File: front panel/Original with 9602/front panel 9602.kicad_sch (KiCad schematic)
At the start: 164 parts, among them J1 Accumulator, J10 Conn_01x04_Female, J11 Conn_01x04_Female, J12 Conn_01x04_Female, J13 ~EXT.LA, J14 Z-BIT, J2 Mem_Buffer, J3 Conn_01x16_Female, J4 Conn_01x04_Female, J5 Conn_01x04_Female, J6 Conn_01x04_Female, J7 SR_REGISTER, J8 Conn_01x04_Female, J9 Conn_01x04_Female, SW1 SR0, SW10 DEPOSIT, SW11 HALT, SW12 SINGLE, SW13 F/S, SW14 PAGE ZERO, SW15 RUN, SW16 EXAM, SW2 SR1, SW3 SR2, SW4 SR3, SW5 SR4, SW6 SR5, SW7 SR6, SW8 SR7, SW9 LD_ADDR, U1 74LS05, U10 DM9602, U11 74LS05, U12 74LS00, U2 74LS05, U3 74LS05, U4 74LS07, U5 74LS07, U6 74LS00, U7 74LS05, U8 74LS00, U9 74LS00

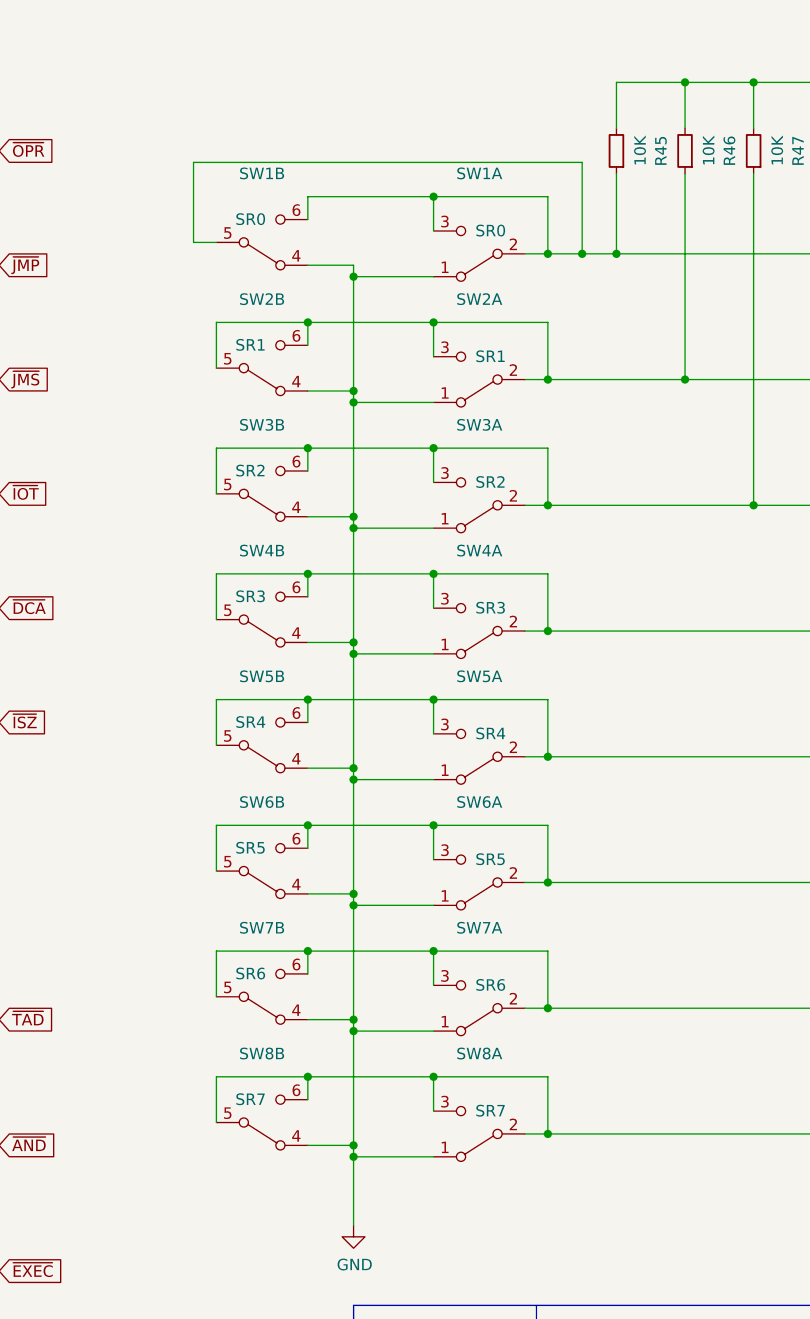
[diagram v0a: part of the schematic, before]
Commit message: New PCB with all the corrections made
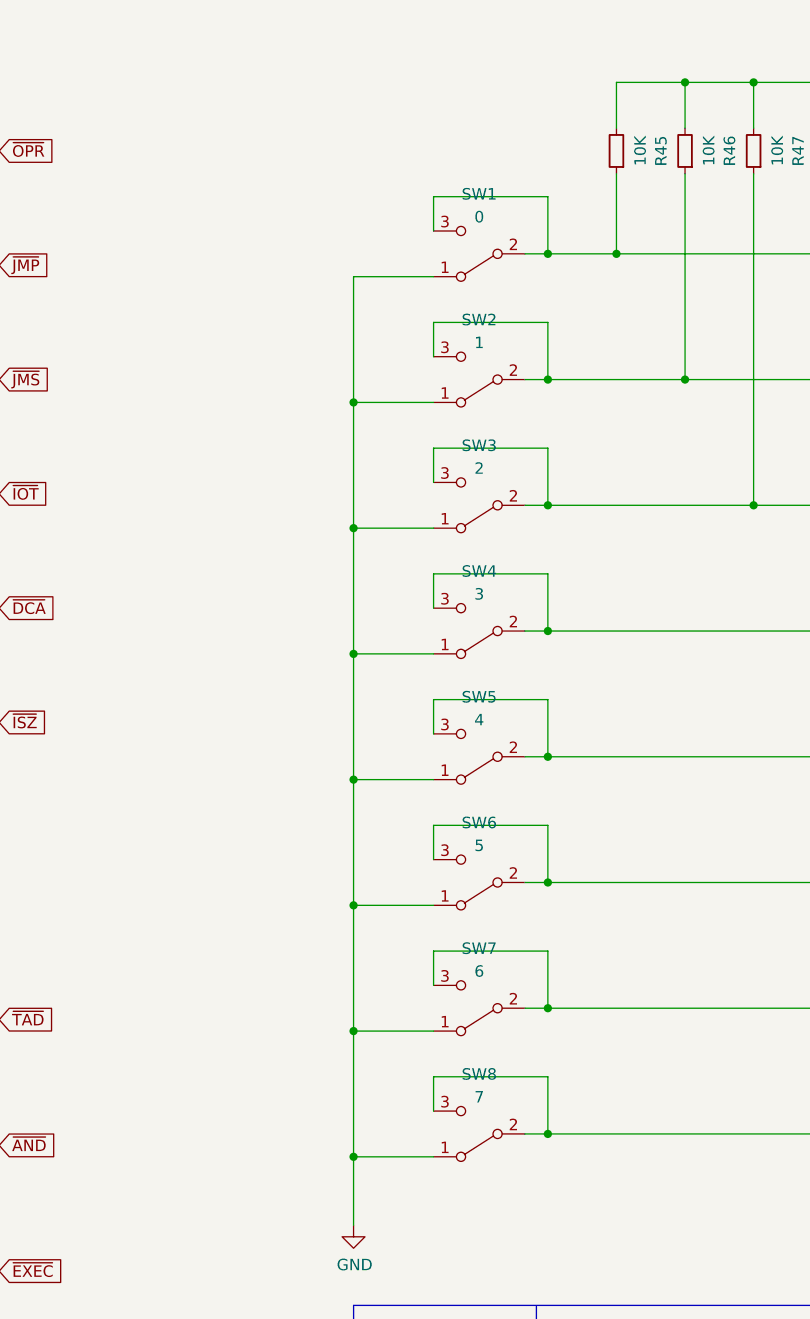
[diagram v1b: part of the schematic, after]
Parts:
- removed SW1: SR0, dBSound_library:DPDT_toggle_switch_wired, symbol Switch:SW_DPDT_x2
- removed SW2: SR1, dBSound_library:DPDT_toggle_switch_wired, symbol Switch:SW_DPDT_x2
- removed SW3: SR2, dBSound_library:DPDT_toggle_switch_wired, symbol Switch:SW_DPDT_x2
- removed SW4: SR3, dBSound_library:DPDT_toggle_switch_wired, symbol Switch:SW_DPDT_x2
- removed SW5: SR4, dBSound_library:DPDT_toggle_switch_wired, symbol Switch:SW_DPDT_x2
- removed SW6: SR5, dBSound_library:DPDT_toggle_switch_wired, symbol Switch:SW_DPDT_x2
- removed SW7: SR6, dBSound_library:DPDT_toggle_switch_wired, symbol Switch:SW_DPDT_x2
- removed SW8: SR7, dBSound_library:DPDT_toggle_switch_wired, symbol Switch:SW_DPDT_x2
- added SW1: 0, EDUC-8:SPDT_toggle_switch_wired, symbol Switch:SW_SPDT
- added SW2: 1, EDUC-8:SPDT_toggle_switch_wired, symbol Switch:SW_SPDT
- added SW3: 2, EDUC-8:SPDT_toggle_switch_wired, symbol Switch:SW_SPDT
- added SW4: 3, EDUC-8:SPDT_toggle_switch_wired, symbol Switch:SW_SPDT
- added SW5: 4, EDUC-8:SPDT_toggle_switch_wired, symbol Switch:SW_SPDT
- added SW6: 5, EDUC-8:SPDT_toggle_switch_wired, symbol Switch:SW_SPDT
- added SW7: 6, EDUC-8:SPDT_toggle_switch_wired, symbol Switch:SW_SPDT
- added SW8: 7, EDUC-8:SPDT_toggle_switch_wired, symbol Switch:SW_SPDT
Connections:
- net GND: now also SW1.1 (A), SW2.1 (A), SW3.1 (A), SW4.1 (A), SW5.1 (A), SW6.1 (A), SW7.1 (A), SW8.1 (A)
- net SR0: now also SW1.2 (B), SW1.3 (C)
- net SR1: now also SW2.2 (B), SW2.3 (C)
- net SR2: now also SW3.2 (B), SW3.3 (C)
- net SR3: now also SW4.2 (B), SW4.3 (C)
- net SR4: now also SW5.2 (B), SW5.3 (C)
- net SR5: now also SW6.2 (B), SW6.3 (C)
- net SR6: now also SW7.2 (B), SW7.3 (C)
- net SR7: now also SW8.2 (B), SW8.3 (C)

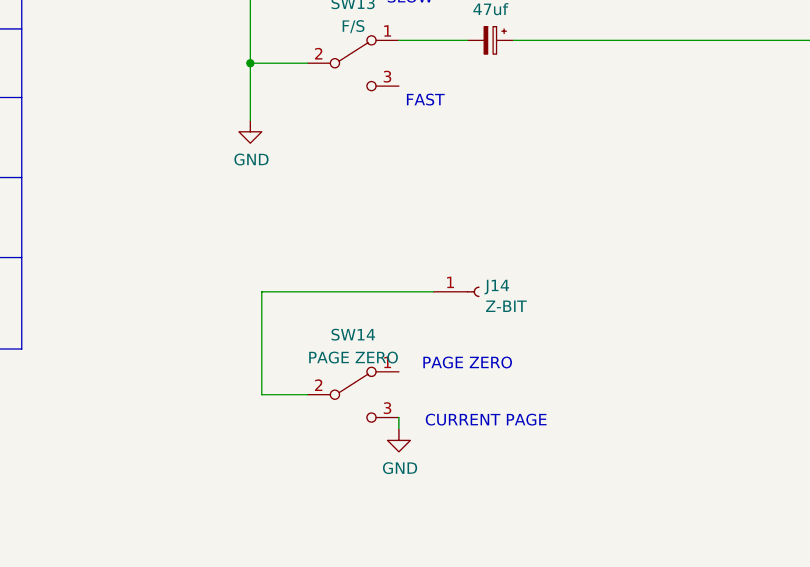
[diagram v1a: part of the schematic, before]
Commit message: Schematic update 2024-04-14 plus fixes
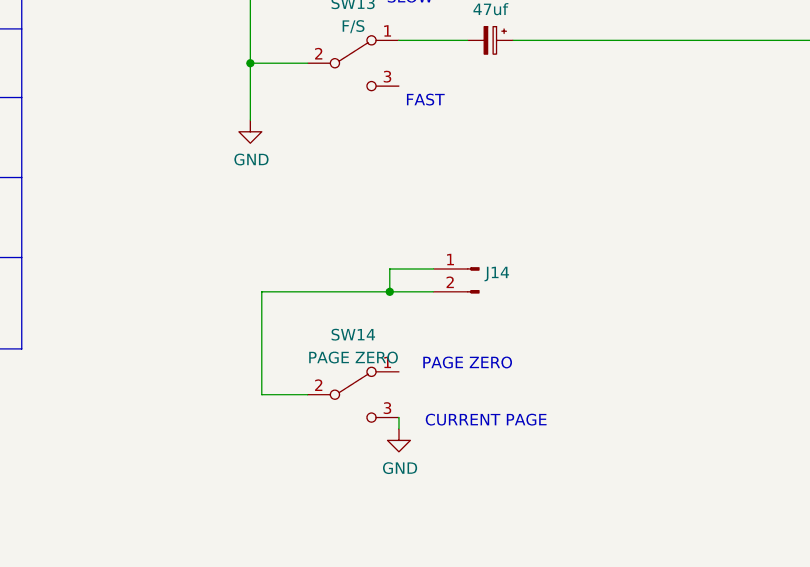
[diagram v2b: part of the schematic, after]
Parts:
- removed J14: Z-BIT, Connector_PinSocket_2.54mm:PinSocket_1x01_P2.54mm_Vertical, symbol Connector:Conn_01x01_Female
- added J14: (no value), symbol Connector:Conn_01x02_Male
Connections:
- net at SW14.2 (B): now also J14.1 (Pin_1), J14.2 (Pin_2)
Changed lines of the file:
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@@
   (junction (at 452.12 38.1) (diameter 0) (color 0 0 0 0)
   )
+  (junction (at 401.574 273.05) (diameter 0) (color 0 0 0 0)
+  )
   (junction (at 323.85 26.67) (diameter 0) (color 0 0 0 0)
   )
@@
     (stroke (width 0) (type default) (color 0 0 0 0))
   )
+  (wire (pts (xy 406.4 270.51) (xy 401.574 270.51))
+    (stroke (width 0) (type default) (color 0 0 0 0))
+  )
   (wire (pts (xy 257.81 118.11) (xy 248.92 118.11))
     (stroke (width 0) (type default) (color 0 0 0 0))
@@
     (stroke (width 0) (type default) (color 0 0 0 0))
   )
+  (wire (pts (xy 401.574 273.05) (xy 406.4 273.05))
+    (stroke (width 0) (type default) (color 0 0 0 0))
+  )
   (wire (pts (xy 110.49 130.81) (xy 107.95 130.81))
     (stroke (width 0) (type default) (color 0 0 0 0))
@@
     (stroke (width 0) (type default) (color 0 0 0 0))
   )
-  (wire (pts (xy 387.35 273.05) (xy 406.4 273.05))
+  (wire (pts (xy 387.35 273.05) (xy 401.574 273.05))
     (stroke (width 0) (type default) (color 0 0 0 0))
   )
@@
     (stroke (width 0) (type default) (color 0 0 0 0))
   )
+  (wire (pts (xy 401.574 270.51) (xy 401.574 273.05))
+    (stroke (width 0) (type default) (color 0 0 0 0))
+  )
   (wire (pts (xy 450.85 54.61) (xy 450.85 60.96))
     (stroke (width 0) (type default) (color 0 0 0 0))
@@
     (pin "1")
   )
-  (symbol (lib_id "Connector:Conn_01x01_Female") (at 411.48 273.05 0) (unit 1)
-    (in_bom yes) (on_board yes)
-    (property "Reference" "J14" (id 0) (at 412.1912 272.3896 0)
-      (effects (font (size 1.27 1.27)) (justify left))
-    )
-    (property "Value" "Z-BIT" (id 1) (at 412.1912 274.701 0)
-      (effects (font (size 1.27 1.27)) (justify left))
-    )
-    (property "Footprint" "Connector_PinSocket_2.54mm:PinSocket_1x01_P2.54mm_Vertical" (id 2) (at 411.48 273.05 0)
-      (effects (font (size 1.27 1.27)) hide)
-    )
-    (property "Datasheet" "~" (id 3) (at 411.48 273.05 0)
-      (effects (font (size 1.27 1.27)) hide)
-    )
-    (pin "1")
-  )
   (symbol (lib_id "Mechanical:MountingHole") (at 127 368.3 0) (unit 1)
     (in_bom yes) (on_board yes)
@@
     (pin "3")
   )
+  (symbol (lib_id "Connector:Conn_01x02_Male") (at 411.48 270.51 0) (mirror y) (unit 1)
+    (in_bom yes) (on_board yes) (fields_autoplaced)
+    (property "Reference" "J14" (id 0) (at 412.1912 270.9453 0)
+      (effects (font (size 1.27 1.27)) (justify right))
+    )
+    (property "Value" "" (id 1) (at 412.1912 273.4822 0)
+      (effects (font (size 1.27 1.27)) (justify right))
+    )
+    (property "Footprint" "" (id 2) (at 411.48 270.51 0)
+      (effects (font (size 1.27 1.27)) hide)
+    )
+    (property "Datasheet" "~" (id 3) (at 411.48 270.51 0)
+      (effects (font (size 1.27 1.27)) hide)
+    )
+    (pin "1")
+    (pin "2")
+  )
   (symbol (lib_id "Switch:SW_SPDT") (at 262.89 87.63 180) (unit 1)
     (in_bom yes) (on_board yes) (fields_autoplaced)
@@
       (reference "J13") (unit 1) (value "~EXT.LA") (footprint "Connector_PinSocket_2.54mm:PinSocket_1x01_P2.54mm_Vertical")
     )
-    (path "/00000000-0000-0000-0000-0000611d623c"
-      (reference "J14") (unit 1) (value "Z-BIT") (footprint "Connector_PinSocket_2.54mm:PinSocket_1x01_P2.54mm_Vertical")
+    (path "/145bc971-852e-4102-a855-052328f4ba92"
+      (reference "J14") (unit 1) (value "Conn_01x02_Male") (footprint "Connector_JST:JST_XH_B2B-XH-A_1x02_P2.50mm_Vertical")
     )
     (path "/00000000-0000-0000-0000-00006037db22"
